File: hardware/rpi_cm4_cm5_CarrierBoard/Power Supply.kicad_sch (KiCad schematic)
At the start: 102 parts, among them Q2 2N7002, Q3 2N7002, Q7 2N7002, U10 TPS54527DDAR, U11 TPS54527DDAR, U12 TPS7A7001DDAR, U13 INA180A2IDBVR, U14 INA180A2IDBVR, U2 SN74LVC1G14DBVR, U28 INA180A2IDBVR, U29 INA180A2IDBVR, U3 SE555DR, U9 TPS54527DDAR

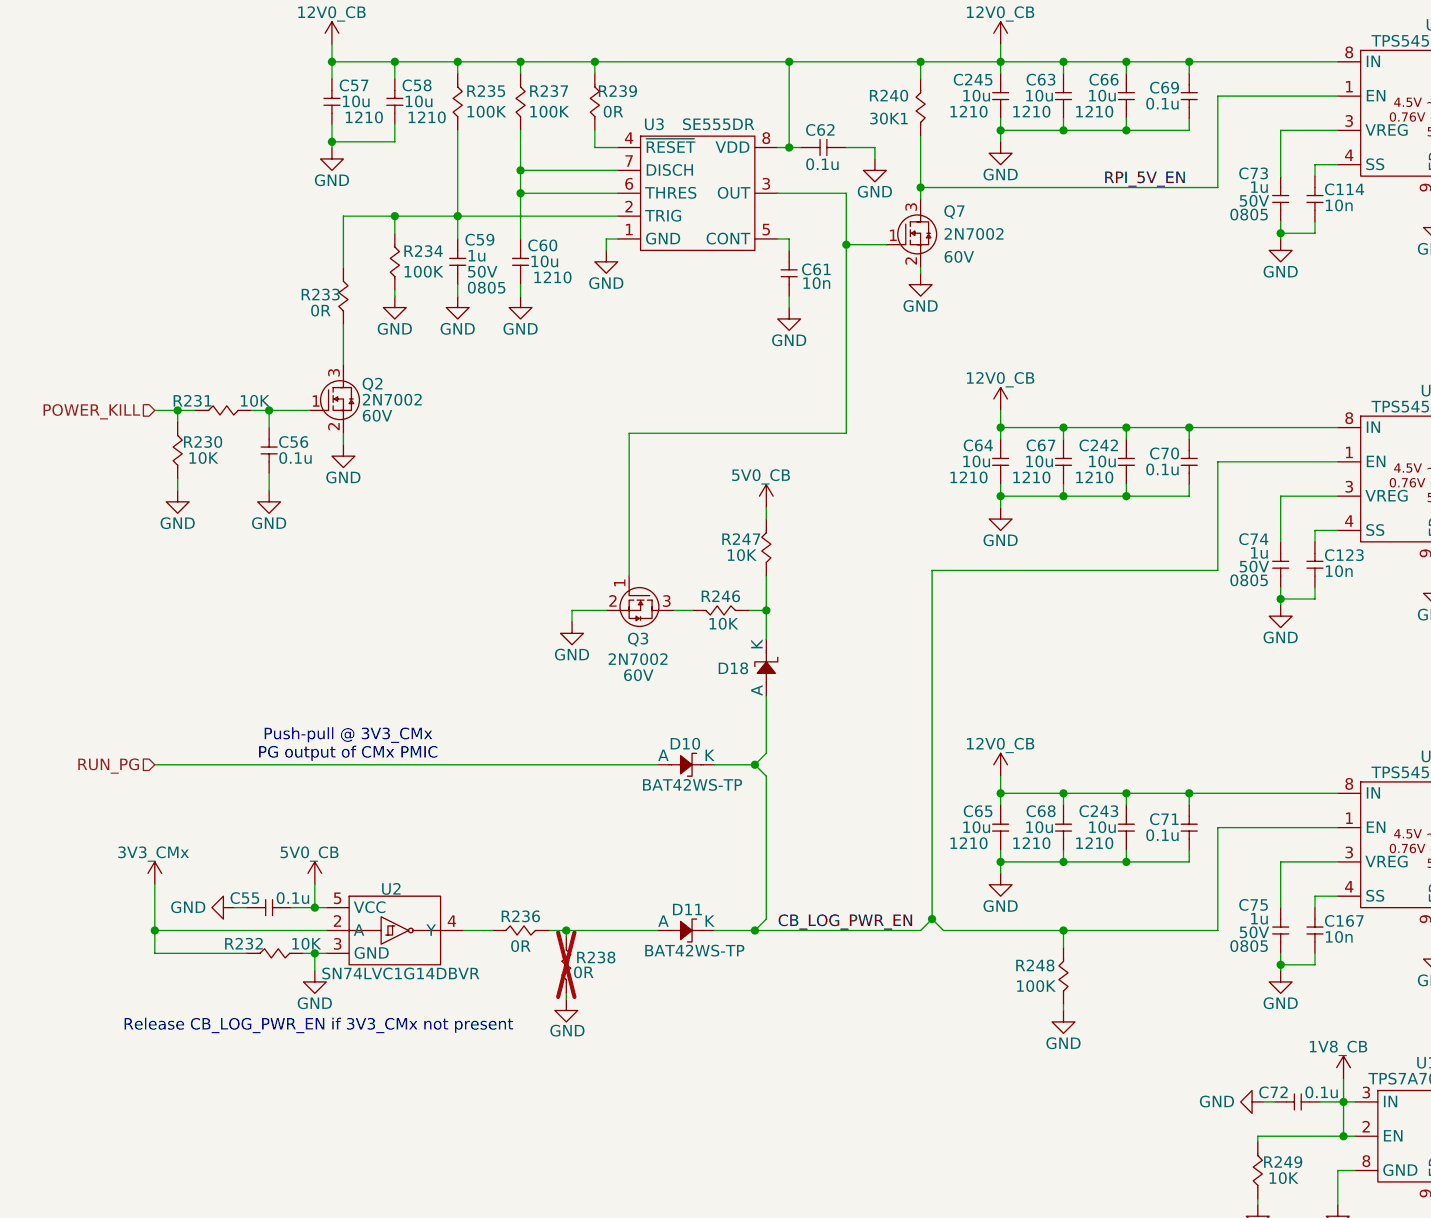
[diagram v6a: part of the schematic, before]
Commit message: Update watchdog timer circuit to add external watchdog timer IC to be fed by PIC Adjust reset scheme in power supply sheet accordingly Adjust PinMux, regen BOM and PDF schematics (preliminary) Start preliminary component placement in the PCB
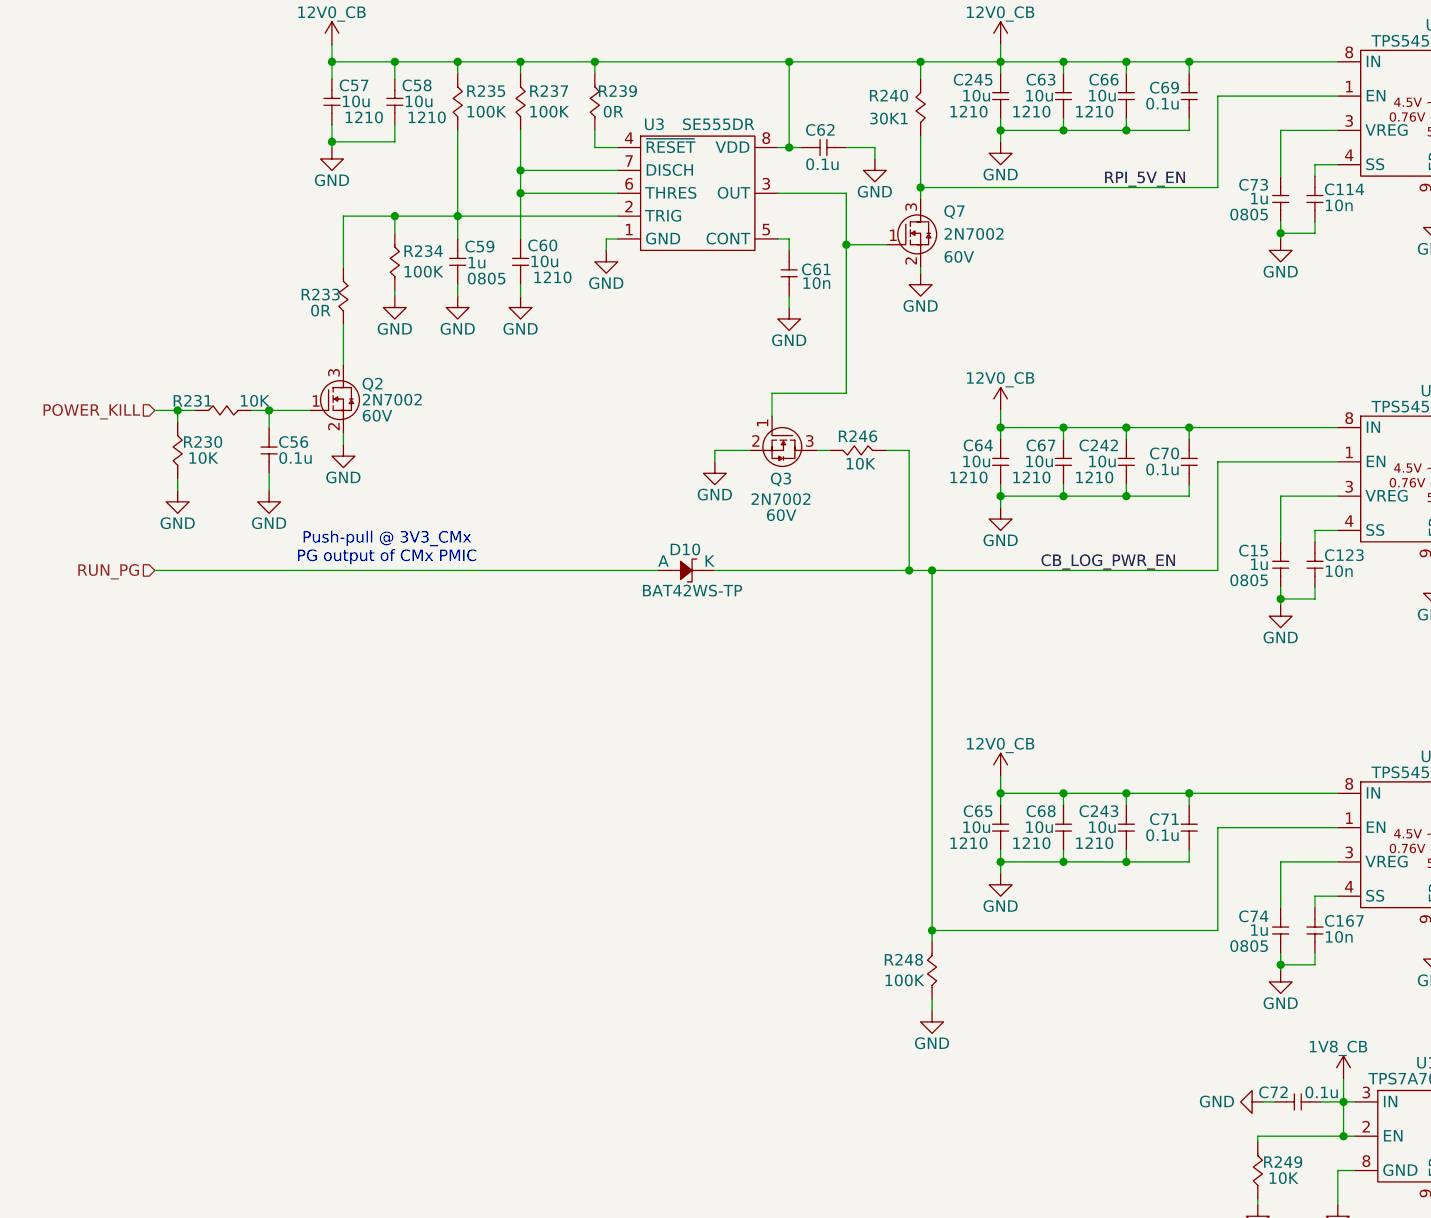
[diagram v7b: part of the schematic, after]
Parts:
- removed C55: 0.1u, footprint:CAP_NONPOL_0402, symbol KicadCompDb:Capacitors/CAP_CER_SMT_00001
- removed C75: 1u, footprint:CAP_NONPOL_0805, symbol KicadCompDb:Capacitors/CAP_CER_SMT_00002
- removed D11, D18: BAT42WS-TP, footprint:SOD-323, symbol KicadCompDb:Diodes/DIODE_00006
- removed R232, R247: 10K, footprint:RES_0402, symbol KicadCompDb:Resistors/RES_SMT_00013
- removed R236, R238: 0R, footprint:RES_0402, symbol KicadCompDb:Resistors/RES_SMT_00001
- removed U2: SN74LVC1G14DBVR, footprint:SOT-23-5, symbol KicadCompDb:Logic/LOGIC_00003
- added C15: 1u, footprint:CAP_NONPOL_0805, symbol KicadCompDb:Capacitors/CAP_CER_SMT_00002
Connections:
- net CB_LOG_PWR_EN: now also R246.1
- net GND: now also C15.1
- net at U10.3 (VREG): now also C15.2; no longer C74.2
- net at U11.3 (VREG): now also C74.2
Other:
- note removed: "Release CB_LOG_PWR_EN if 3V3_CMx not present"
- moved on the sheet: D10, Q3, R246, R248

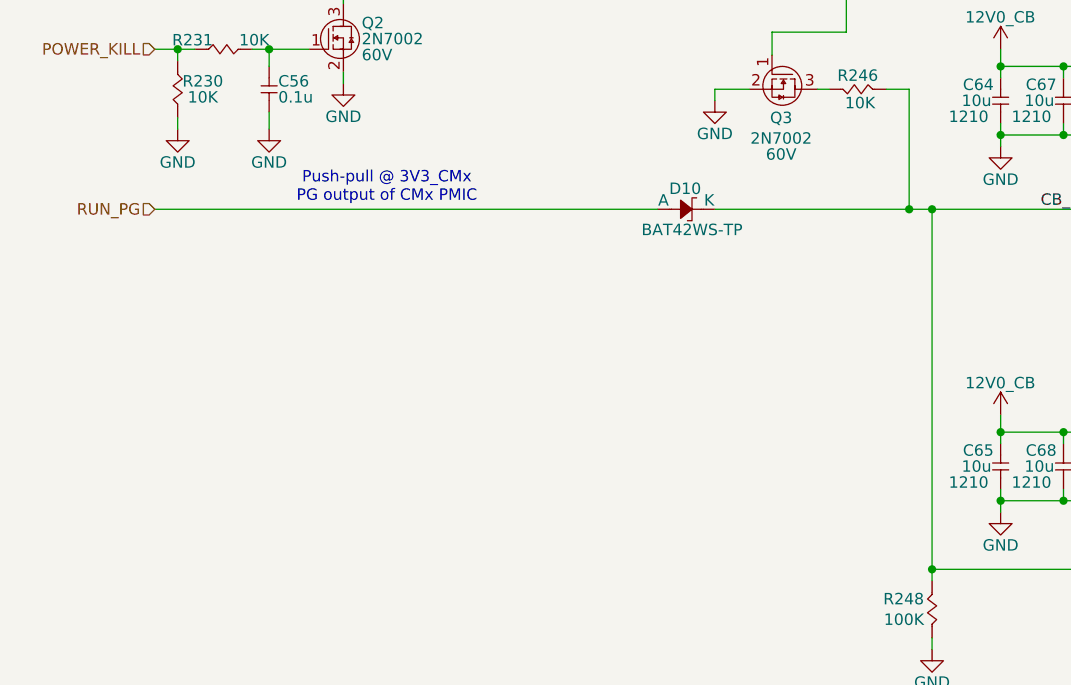
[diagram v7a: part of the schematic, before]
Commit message: Review watchdog timer circuit to prevent race condition during shutdown
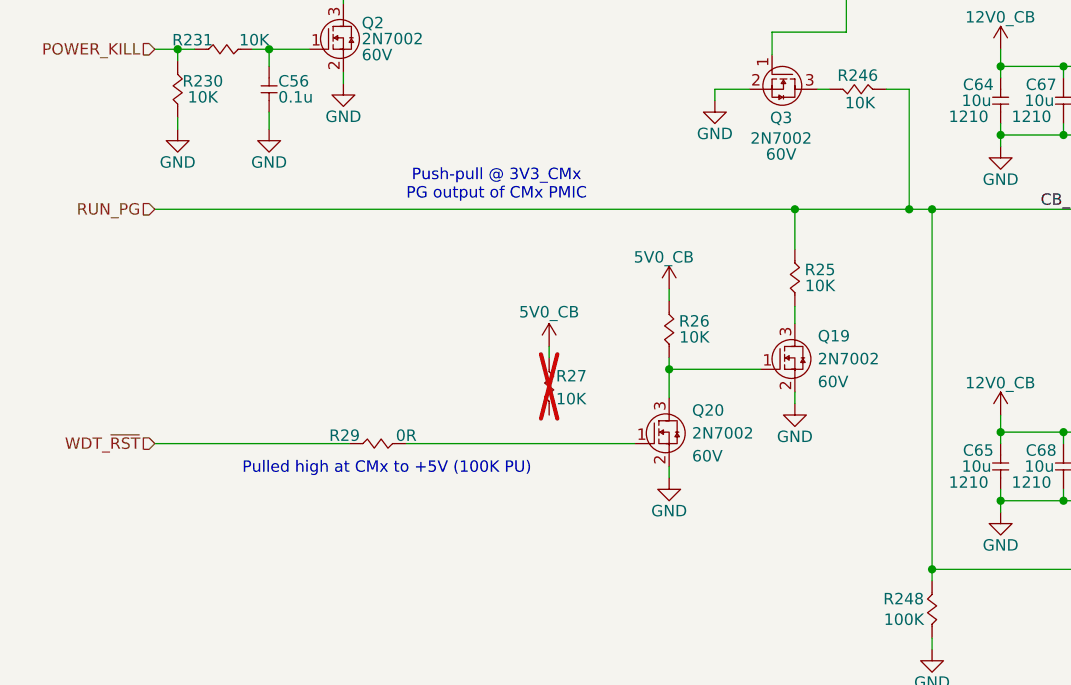
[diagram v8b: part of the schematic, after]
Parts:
- removed D10: BAT42WS-TP, footprint:SOD-323, symbol KicadCompDb:Diodes/DIODE_00006
- added Q19, Q20: 2N7002, footprint:SOT-23-3, symbol KicadCompDb:Mosfet/MOSFET_00001
- added R25, R26, R27: 10K, footprint:RES_0402, symbol KicadCompDb:Resistors/RES_SMT_00013
- added R29: 0R, footprint:RES_0402, symbol KicadCompDb:Resistors/RES_SMT_00001
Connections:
- net CB_LOG_PWR_EN is gone; now on net RUN_PG: R246.1, R248.2, U10.1 (EN), U11.1 (EN)
- net 5V0_CB: now also R26.2, R27.2
- net GND: now also Q19.2 (S), Q20.2 (S)
- net RUN_PG: now also R25.2
- new net: Q20.1 (G), R29.1
- new net: Q19.3 (D), R25.1
- new net: Q19.1 (G), Q20.3 (D), R26.1
- new net WDT_~{RST}: R29.2
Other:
- note added: "Pulled high at CMx to +5V (100K PU)"
